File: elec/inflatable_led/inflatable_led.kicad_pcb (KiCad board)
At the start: 2 copper layers, 100.1 x 100 mm, 86 parts, among them J1 Header-Male-2.54_1x20, J2 Conn_01x02_Pin, J3 Conn_01x02_Pin, SW1 TS-1093C-A7B2-D1, U1 RP2040, U2 W25Q128JVSIQTR, U3 TPS61165DRVR, U4 BQ24040DSQR, U5 AMS1117-3.3, U6 F.0603.00026/P2-0603B1TS2-06T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, U7 SI2323DS, X1 X322512MSB4SI

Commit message: whole new circuit
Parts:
- removed BAT1, BAT2: BH-18650-A5BJ003, footprints:BAT-TH_BH-18650-A5BJ003
- removed C13: 10nF, Capacitor_SMD:C_0402_1005Metric
- removed D8, D9: MBR0540T1G, footprints:SOD-123_L2.8-W1.8-LS3.7-RD
- removed SW1: TS-1093C-A7B2-D1, footprints:SW-TH_TS-1093C-A7B3-D1
- removed TP_POWER_OR_1: TestPoint, TestPoint:TestPoint_Pad_D1.5mm
- added BT1: BH-18650-B1BA007, footprints:BAT-SMD_BH-18650-B1BA007, F.Cu at (101.4, 100.0)
- added BTBOOT1: TS-1187A-B-A-B, footprints:SW-SMD_4P-L5.1-W5.1-P3.70-LS6.5-TL-2, F.Cu at (123.8, 70.1)
- added BTUI1: TS-1187A-B-A-B, footprints:SW-SMD_4P-L5.1-W5.1-P3.70-LS6.5-TL-2, F.Cu at (101.4, 75.0)
- added C14: 47nF, Capacitor_SMD:C_0603_1608Metric, F.Cu at (114.4, 127.8)
- added C23: 10uF, Capacitor_SMD:C_0805_2012Metric, F.Cu at (110.4, 122.1)
- added C24: 10uF, Capacitor_SMD:C_0805_2012Metric, F.Cu at (117.1, 128.4)
- added C25: 1uF, Capacitor_SMD:C_0603_1608Metric, F.Cu at (125.0, 76.8)
- added C26: 1uF, Capacitor_SMD:C_0603_1608Metric, F.Cu at (125.0, 78.5)
- added CN1: S2B-PH-SM4-TB(LF)(SN), footprints:CONN-SMD_P2.00_S2B-PH-SM4-TB-LF-SN, F.Cu at (107.6, 140.0)
- added J4: USB4205-GF-A_REVA, footprints:GCT_USB4205-GF-A_REVA, F.Cu at (101.4, 57.8)
- added JP1: SolderJumper_3_Bridged12, Jumper:SolderJumper-3_P1.3mm_Bridged12_RoundedPad1.0x1.5mm, F.Cu at (93.2, 121.5)
- added JP2: SolderJumper_2_Open, Jumper:SolderJumper-2_P1.3mm_Open_TrianglePad1.0x1.5mm, F.Cu at (106.1, 74.9)
- added JP3: SolderJumper_3_Open, Jumper:SolderJumper-3_P2.0mm_Open_TrianglePad1.0x1.5mm, F.Cu at (123.6, 74.3)
- added L2: 1uH/3A, Inductor_SMD:L_1008_2520Metric, F.Cu at (110.8, 126.8)
- added Q1: 2N7002KW_R1_00001, footprints:SOT-323-3_L2.0-W1.3-P1.30-LS2.1-BR, F.Cu at (89.4, 128.2)
- added R17: 10K, Resistor_SMD:R_0402_1005Metric, F.Cu at (112.9, 129.5)
- added R18: 10K, Resistor_SMD:R_0402_1005Metric, F.Cu at (91.9, 124.1)
- added R19: 10k, Resistor_SMD:R_0603_1608Metric, F.Cu at (118.1, 71.7)
- added R20: 10K, Resistor_SMD:R_0402_1005Metric, F.Cu at (89.2, 130.1)
- added TP1: TestPoint, TestPoint:TestPoint_Pad_D1.0mm, F.Cu at (118.2, 74.5)
- added TP2: TestPoint, TestPoint:TestPoint_Pad_D1.0mm, F.Cu at (127.9, 77.6)
- added TP7: TestPoint, TestPoint:TestPoint_Pad_D1.0mm, F.Cu at (118.2, 76.6)
- added TP8: TestPoint, TestPoint:TestPoint_Pad_D1.0mm, F.Cu at (118.2, 78.7)
- added U8: TPS7A0233DQNR, footprints:X2SON-4_L1.0-W1.0-P0.65-TL-EP, F.Cu at (115.2, 132.4)
- C19: value 1uF -> 0.1uF; footprint Capacitor_SMD:C_0805_2012Metric -> Capacitor_SMD:C_0603_1608Metric
- C20, C21: value 100nF -> 1uF; footprint Capacitor_SMD:C_0402_1005Metric -> Capacitor_SMD:C_0805_2012Metric
- J1: value Header-Male-2.54_1x20 -> Conn_01x10; footprint footprints:HDR-TH_20P-P2.54-V-M-1 -> Connector_PinHeader_1.00mm:PinHeader_1x10_P1.00mm_Vertical
- R7: value 600R -> 10K
- U4: value BQ24040DSQR -> BQ25601DRTWR; footprint footprints:WSON-10_L2.0-W2.0-P0.40-BL-EP -> footprints:WQFN-24_L4.0-W4.0-P0.50-TL-EP2.7
- U5: value AMS1117-3.3 -> STM6601GU2BDM6F; footprint footprints:SOT-223-3_L6.5-W3.4-P2.30-LS7.0-BR -> Package_DFN_QFN:TDFN-12_2x3mm_P0.5mm
- moved H4 134.0 mm to (60.0, 22.0)
- moved H2 119.0 mm to (49.0, 23.1)
- moved H3 104.6 mm to (28.1, 21.5)
- moved D5 89.0 mm to (98.1, 141.5), turned to 90 degrees
- moved D6 88.7 mm to (95.3, 141.4), turned to -90 degrees
- moved TP6 75.2 mm to (57.3, 104.6)
- moved D7 67.0 mm to (92.6, 141.4)
- moved TPCC1 65.8 mm to (95.3, 62.2), turned to 180 degrees
- moved R10 64.2 mm to (97.1, 65.2), turned to 180 degrees
- moved D4 54.3 mm to (93.0, 134.7), turned to 90 degrees
- moved U5 52.6 mm to (121.4, 77.8), turned to 180 degrees
- moved H1 52.2 mm to (38.6, 23.4)
- moved USB2 49.7 mm to (114.1, 61.6), turned to 160 degrees
- moved R11 49.5 mm to (105.3, 62.3), turned to 0 degrees
- moved TPCC2 48.9 mm to (106.1, 59.6), turned to 180 degrees
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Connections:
- C19 pad 1: +BATT -> VCC
- C20 pad 1: /POWER_IN_OR -> VCC
- C22 pad 1: /ON_OFF_BT -> /PWR_ON
- J1 pad 1: Net-(U1-GPIO9) -> GND
- J1 pad 10: Net-(U1-GPIO18) -> /GPIO11
- J1 pad 2: Net-(U1-GPIO10) -> +3.3V
- J1 pad 3: Net-(U1-GPIO11) -> +BATT
- J1 pad 4: Net-(U1-GPIO12) -> VCC
- J1 pad 5: Net-(U1-GPIO13) -> VBUS
- J1 pad 6: Net-(U1-GPIO14) -> /PWR_EN
- J1 pad 7: Net-(U1-GPIO15) -> /GPIO8
- J1 pad 8: Net-(U1-GPIO16) -> /GPIO9
- J1 pad 9: Net-(U1-GPIO17) -> /GPIO10
- LED_CHG_2 pad 1: /CHG_CHG -> /CHG_STAT
- R15 pad 2: /ON_OFF_BT -> /PWR_ON
- R16 pad 1: Net-(U7-G) -> /LED_ON
- R16 pad 2: /LED_ON -> Net-(Q1-G)
- R7 pad 1: Net-(U4-ISET) -> /CHG_REGN
- R7 pad 2: GND -> Net-(U4-TS)
- R8 pad 1: +BATT -> VCC
- R9 pad 1: +BATT -> VCC
- TP_LED_ON1 pad 1: Net-(U7-G) -> /LED_ON
- U1 pad 11: unconnected-(U1-GPIO8-Pad11) -> /GPIO8
- U1 pad 12: Net-(U1-GPIO9) -> /GPIO9
- U1 pad 13: Net-(U1-GPIO10) -> /GPIO10
- U1 pad 14: Net-(U1-GPIO11) -> /GPIO11
- U1 pad 15: Net-(U1-GPIO12) -> /GPIO12
- U1 pad 16: Net-(U1-GPIO13) -> /GPIO13
- U1 pad 17: Net-(U1-GPIO14) -> /PWR_HOLD
- U1 pad 18: Net-(U1-GPIO15) -> /PWR_LOW
- U1 pad 2: unconnected-(U1-GPIO0-Pad2) -> /DIM_CTRL
- U1 pad 27: Net-(U1-GPIO16) -> /BTN1
- U1 pad 28: Net-(U1-GPIO17) -> /GPIO17
- U1 pad 29: Net-(U1-GPIO18) -> /GPIO18
- U1 pad 3: unconnected-(U1-GPIO1-Pad3) -> /LED_ON
- U1 pad 30: Net-(U1-GPIO19) -> unconnected-(U1-GPIO19-Pad30)
- U1 pad 31: Net-(U1-GPIO20) -> unconnected-(U1-GPIO20-Pad31)
- U1 pad 32: Net-(U1-GPIO21) -> unconnected-(U1-GPIO21-Pad32)
- U1 pad 34: Net-(U1-GPIO22) -> unconnected-(U1-GPIO22-Pad34)
- U1 pad 35: Net-(U1-GPIO23) -> unconnected-(U1-GPIO23-Pad35)
- U1 pad 36: Net-(U1-GPIO24) -> unconnected-(U1-GPIO24-Pad36)
- U1 pad 37: Net-(U1-GPIO25) -> unconnected-(U1-GPIO25-Pad37)
- U1 pad 38: Net-(U1-GPIO26_ADC0) -> unconnected-(U1-GPIO26_ADC0-Pad38)
- U1 pad 39: Net-(U1-GPIO27_ADC1) -> unconnected-(U1-GPIO27_ADC1-Pad39)
- U1 pad 4: unconnected-(U1-GPIO2-Pad4) -> /CHG_QON
- U1 pad 40: Net-(U1-GPIO28_ADC2) -> unconnected-(U1-GPIO28_ADC2-Pad40)
- U1 pad 5: /LED_ON -> /CHG_INT
- U1 pad 6: /DIM_CTRL -> /SDA
- U1 pad 7: /ON_OFF_BT -> /SCL
- U1 pad 8: unconnected-(U1-GPIO6-Pad8) -> /CHG_STAT
- U1 pad 9: unconnected-(U1-GPIO7-Pad9) -> /CHG_PG
- U4 pad 10: +BATT -> unconnected-(U4-NC-Pad10)
- U4 pad 11: GND -> Net-(U4-TS)
- U4 pad 2: Net-(U4-ISET) -> VBUS
- U4 pad 3: GND -> /CHG_PG
- U4 pad 4: unconnected-(U4-PRETERM-Pad4) -> /CHG_STAT
- U4 pad 5: /CHG_PG -> /SCL
- U4 pad 6: unconnected-(U4-NC-Pad6) -> /SDA
- U4 pad 7: VBUS -> /CHG_INT
- U4 pad 8: /CHG_CHG -> unconnected-(U4-NC-Pad8)
- U4 pad 9: unconnected-(U4-TS-Pad9) -> GND
- U5 pad 1: GND -> VCC
- U5 pad 2: +3.3V -> /PWR_SR
- U5 pad 3: /POWER_IN_OR -> Net-(U5-VREF)
- U5 pad 4: +3.3V -> /PWR_HOLD
- U7 pad 1: Net-(U7-G) -> Net-(Q1-D)
- U7 pad 2: +BATT -> Net-(JP1-C)
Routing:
- net +3.3V: track 222.6 -> 31.7 mm, vias 7 -> 15
- net VCC: track 0.00 -> 90.1 mm, vias 0 -> 9
- net /PWR_EN: track 0.00 -> 75.7 mm, vias 0 -> 2
- net /ON_OFF_BT: track 74.7 -> 0.00 mm, vias 1 -> 0
- net Net-(D4-K): track 82.1 -> 7.55 mm
- net /CHG_STAT: track 0.00 -> 61.3 mm
- net Net-(U1-GPIO9): track 60.3 -> 0.00 mm
- net /DIM_CTRL: track 112.7 -> 52.5 mm, vias 4 -> 2
- net /CHG_PG: track 4.18 -> 62.7 mm, vias 2 -> 0
- net /SCL: track 0.00 -> 58.5 mm
- net /LED_ON: track 113.8 -> 55.4 mm, vias 2 -> 0
- net Net-(U1-GPIO10): track 58.1 -> 0.00 mm
- net /SDA: track 0.00 -> 57.3 mm
- net /CHG_INT: track 0.00 -> 56.3 mm
- net /CHG_QON: track 0.00 -> 55.6 mm, vias 0 -> 2
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- added copper zone on F.Cu, net +3.3V
- added copper zone on In1.Cu, net +3.3V
- added copper zone on F.Cu, net +BATT
- added copper zone on In2.Cu, net +BATT
- added copper zone on In2.Cu, net VBUS
- added copper zone on In2.Cu, net VCC
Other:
- board size 100.1 x 100 mm -> 91.8 x 92 mm
- copper layers 2 -> 4
- board text added: "Boot"
- board text added: "Reset"

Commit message: update bom
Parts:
- C19: value 0.1uF -> 100nF; footprint Capacitor_SMD:C_0603_1608Metric -> Capacitor_SMD:C_0402_1005Metric
- C25, C26: footprint Capacitor_SMD:C_0603_1608Metric -> Capacitor_SMD:C_0805_2012Metric
- R19: footprint Resistor_SMD:R_0603_1608Metric -> Resistor_SMD:R_0402_1005Metric
- moved H3 149.8 mm to (131.4, 130.0)
- moved H4 108.6 mm to (71.4, 130.0)
- moved H1 103.8 mm to (131.4, 70.0)
- moved H2 52.0 mm to (71.4, 70.0)
- moved J3 0.60 mm to (130.6, 124.3)
- moved C1 0.57 mm to (94.6, 79.0)
- moved C25 0.55 mm to (124.9, 76.2)
- moved U5 0.51 mm to (121.3, 77.3)
- moved C5 0.50 mm to (80.3, 78.6)
- moved JP3 0.33 mm to (123.6, 74.0)
- moved C26 0.25 mm to (125.0, 78.2)
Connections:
- U1 pad 28: /GPIO17 -> unconnected-(U1-GPIO17-Pad28)
- U1 pad 29: /GPIO18 -> unconnected-(U1-GPIO18-Pad29)
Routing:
- net /PWR_ON: track 19.2 -> 38.3 mm, vias 0 -> 2
- net /QSPI_SS: track 58.8 -> 42.3 mm, vias 0 -> 2
- net +BATT: track 57.7 -> 50.3 mm, vias 31 -> 30
- net GND: track 44.0 -> 45.8 mm, vias 67 -> 68
- net /PWR_SR: track 9.45 -> 10.9 mm
- net /osc_in: track 10.5 -> 9.80 mm
- net /BTN1: track 39.0 -> 38.3 mm
- net /PWR_EN: track 75.7 -> 75.2 mm
- net VCC: track 90.1 -> 90.6 mm
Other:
- outline, holes or cut-outs redrawn

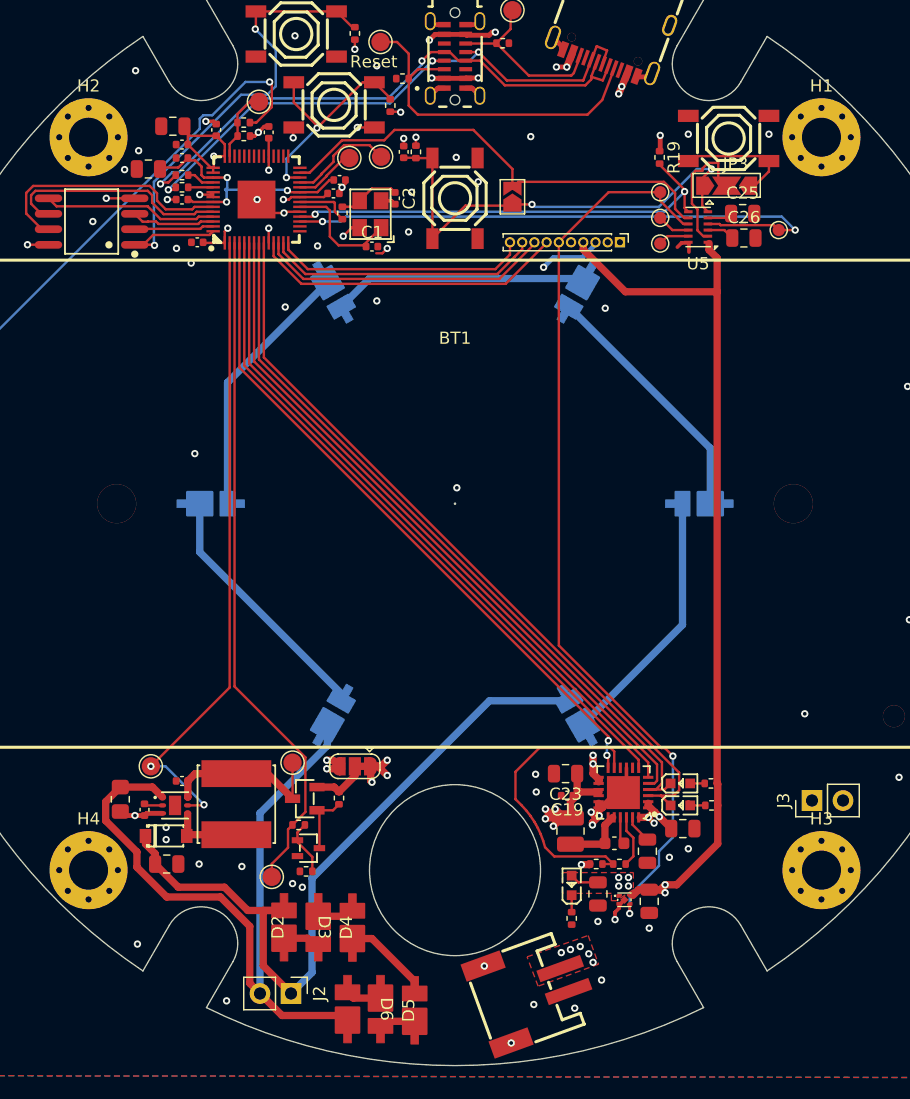
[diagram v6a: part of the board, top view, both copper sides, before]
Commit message: fix additional parts in BOM
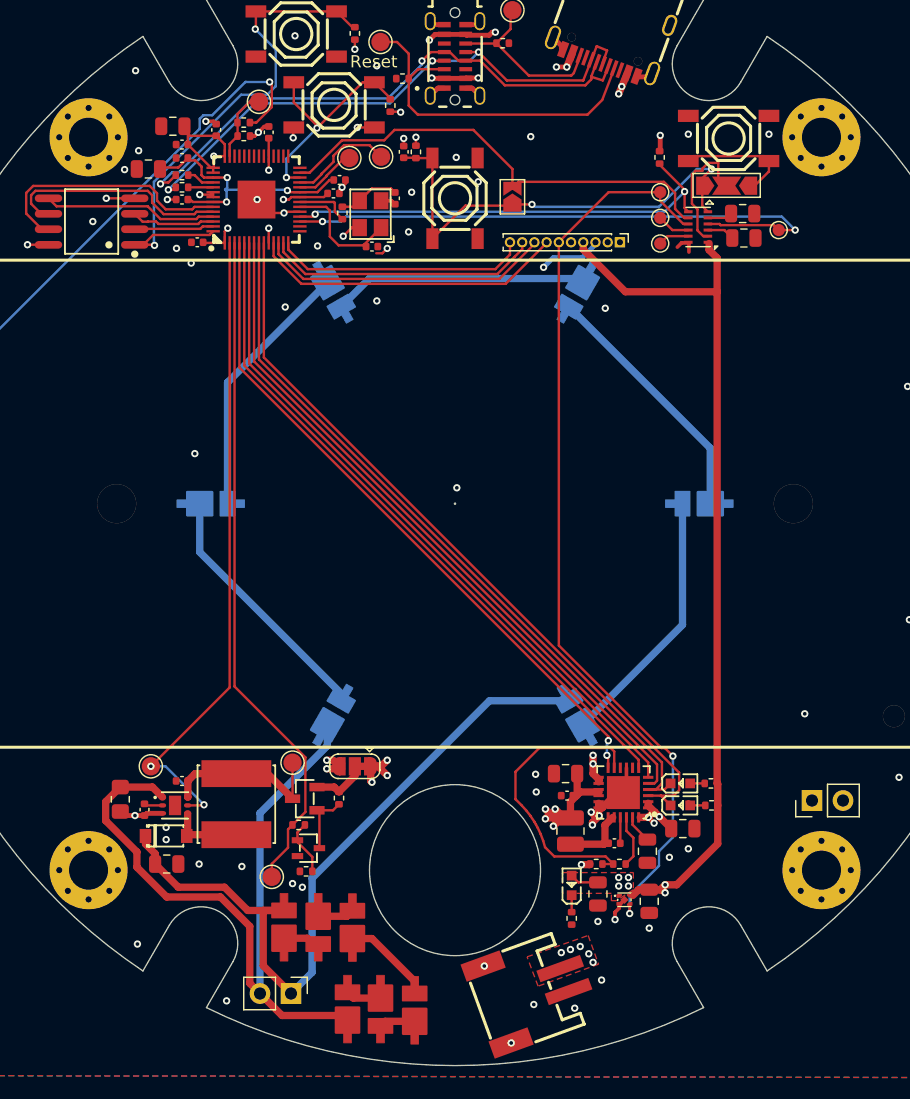
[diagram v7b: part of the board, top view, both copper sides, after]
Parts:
- C14: footprint Capacitor_SMD:C_0603_1608Metric -> Capacitor_SMD:C_0402_1005Metric
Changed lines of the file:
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@@
 			(at 0 -4.2 0)
 			(layer "F.SilkS")
+			(hide yes)
 			(effects
 				(font
@@
 			(at 0.725 -1.775 0)
 			(layer "F.SilkS")
+			(hide yes)
 			(effects
 				(font
@@
 			(at 0 -1.17 -90)
 			(layer "F.SilkS")
+			(hide yes)
 			(effects
 				(font
@@
 			(at 0 -1.68 0)
 			(layer "F.SilkS")
+			(hide yes)
 			(effects
 				(font
@@
 			(at 0 -1.16 180)
 			(layer "F.SilkS")
+			(hide yes)
 			(effects
 				(font
@@
 			(at 0 -3 180)
 			(layer "F.SilkS")
+			(hide yes)
 			(effects
 				(font
@@
 			(at 0 -13.55 0)
 			(layer "F.SilkS")
+			(hide yes)
 			(effects
 				(font
@@
 		)
 	)
-	(footprint "Capacitor_SMD:C_0603_1608Metric"
+	(footprint "Capacitor_SMD:C_0402_1005Metric"
 		(layer "F.Cu")
 		(at 114.42 127.8 180)
-		(descr "Capacitor SMD 0603 (1608 Metric), square (rectangular) end terminal, IPC_7351 nominal, (Body size source: IPC-SM-782 page 76, https://www.pcb-3d.com/wordpress/wp-content/uploads/ipc-sm-782a_amendment_1_and_2.pdf), generated with kicad-footprint-generator")
+		(descr "Capacitor SMD 0402 (1005 Metric), square (rectangular) end terminal, IPC_7351 nominal, (Body size source: IPC-SM-782 page 76, https://www.pcb-3d.com/wordpress/wp-content/uploads/ipc-sm-782a_amendment_1_and_2.pdf), generated with kicad-footprint-generator")
 		(tags "capacitor")
 		(property "Reference" "C14"
-			(at 0 -1.43 180)
+			(at 0 -1.16 180)
 			(layer "F.SilkS")
 			(hide yes)
@@
 		)
 		(property "Value" "47nF"
-			(at 0 1.43 180)
+			(at 0 1.16 180)
 			(layer "F.Fab")
 			(effects
@@
 			)
 		)
-		(property "Footprint" "Capacitor_SMD:C_0603_1608Metric"
+		(property "Footprint" "Capacitor_SMD:C_0402_1005Metric"
 			(at 0 0 180)
 			(unlocked yes)
@@
 			)
 		)
-		(property "LCSC Part" "C77012"
+		(property "LCSC Part" "C272875"
 			(at 0 0 180)
 			(unlocked yes)
@@
 		(attr smd)
 		(fp_line
-			(start -0.14058 0.51)
-			(end 0.14058 0.51)
+			(start -0.107836 0.36)
+			(end 0.107836 0.36)
 			(stroke
 				(width 0.12)
@@
 		)
 		(fp_line
-			(start -0.14058 -0.51)
-			(end 0.14058 -0.51)
+			(start -0.107836 -0.36)
+			(end 0.107836 -0.36)
 			(stroke
 				(width 0.12)
@@
 		)
 		(fp_line
-			(start 1.48 0.73)
-			(end -1.48 0.73)
+			(start 0.91 0.46)
+			(end -0.91 0.46)
 			(stroke
 				(width 0.05)
@@
 		)
 		(fp_line
-			(start 1.48 -0.73)
-			(end 1.48 0.73)
+			(start 0.91 -0.46)
+			(end 0.91 0.46)
 			(stroke
 				(width 0.05)
@@
 		)
 		(fp_line
-			(start -1.48 0.73)
-			(end -1.48 -0.73)
+			(start -0.91 0.46)
+			(end -0.91 -0.46)
 			(stroke
 				(width 0.05)
@@
 		)
 		(fp_line
-			(start -1.48 -0.73)
-			(end 1.48 -0.73)
+			(start -0.91 -0.46)
+			(end 0.91 -0.46)
 			(stroke
 				(width 0.05)
@@
 		)
 		(fp_line
-			(start 0.8 0.4)
-			(end -0.8 0.4)
+			(start 0.5 0.25)
+			(end -0.5 0.25)
 			(stroke
 				(width 0.1)
@@
 		)
 		(fp_line
-			(start 0.8 -0.4)
-			(end 0.8 0.4)
+			(start 0.5 -0.25)
+			(end 0.5 0.25)
 			(stroke
 				(width 0.1)
@@
 		)
 		(fp_line
-			(start -0.8 0.4)
-			(end -0.8 -0.4)
+			(start -0.5 0.25)
+			(end -0.5 -0.25)
 			(stroke
 				(width 0.1)
@@
 		)
 		(fp_line
-			(start -0.8 -0.4)
-			(end 0.8 -0.4)
+			(start -0.5 -0.25)
+			(end 0.5 -0.25)
 			(stroke
 				(width 0.1)
@@
 			(effects
 				(font
-					(size 0.4 0.4)
-					(thickness 0.06)
+					(size 0.25 0.25)
+					(thickness 0.04)
 				)
 			)
 		)
 		(pad "1" smd roundrect
-			(at -0.775 0 180)
-			(size 0.9 0.95)
+			(at -0.48 0 180)
+			(size 0.56 0.62)
 			(layers "F.Cu" "F.Paste" "F.Mask")
 			(roundrect_rratio 0.25)
@@
 		)
 		(pad "2" smd roundrect
-			(at 0.775 0 180)
-			(size 0.9 0.95)
+			(at 0.48 0 180)
+			(size 0.56 0.62)
 			(layers "F.Cu" "F.Paste" "F.Mask")
 			(roundrect_rratio 0.25)
@@
 			(pintype "passive")
 		)
-		(model "${KICAD8_3DMODEL_DIR}/Capacitor_SMD.3dshapes/C_0603_1608Metric.wrl"
+		(model "${KICAD8_3DMODEL_DIR}/Capacitor_SMD.3dshapes/C_0402_1005Metric.wrl"
 			(offset
 				(xyz 0 0 0)
@@
 		(sheetname "Root")
 		(sheetfile "inflatable_led.kicad_sch")
-		(attr smd dnp)
+		(attr smd)
 		(fp_line
 			(start -0.153641 0.38)
@@
 			(at 0 -4.2 0)
 			(layer "F.SilkS")
+			(hide yes)
 			(effects
 				(font
@@
 			(at 0 -1.68 180)
 			(layer "F.SilkS")
+			(hide yes)
 			(effects
 				(font
@@
 			(at 0 -4.2 0)
 			(layer "F.SilkS")
+			(hide yes)
 			(effects
 				(font
@@
 			(at 0 -2.33 -90)
 			(layer "F.SilkS")
+			(hide yes)
 			(effects
 				(font
@@
 			(unlocked yes)
 			(layer "F.SilkS")
+			(hide yes)
 			(effects
 				(font
@@
 			(at 0 -4.2 0)
 			(layer "F.SilkS")
+			(hide yes)
 			(effects
 				(font
@@
 			)
 		)
-		(property "LCSC Part" "C21353"
+		(property "LCSC Part" "C109213"
 			(at 0 0 0)
 			(unlocked yes)
@@
 			(unlocked yes)
 			(layer "F.SilkS")
+			(hide yes)
 			(effects
 				(font
@@
 			(at 0 -1.68 0)
 			(layer "F.SilkS")
+			(hide yes)
 			(effects
 				(font
@@
 			(at 0 -1.16 0)
 			(layer "F.SilkS")
+			(hide yes)
 			(effects
 				(font
@@
 			(at 0 -2.33 90)
 			(layer "F.SilkS")
+			(hide yes)
 			(effects
 				(font
@@
 			(unlocked yes)
 			(layer "F.SilkS")
+			(hide yes)
 			(effects
 				(font
@@
 			(at 0 -1.16 90)
 			(layer "F.SilkS")
+			(hide yes)
 			(effects
 				(font
@@
 			(unlocked yes)
 			(layer "F.SilkS")
+			(hide yes)
 			(effects
 				(font
@@
 			(unlocked yes)
 			(layer "F.SilkS")
+			(hide yes)
 			(effects
 				(font
@@
 	)
 	(segment
-		(start 114.905 127.51)
-		(end 115.195 127.8)
-		(width 0.2)
-		(layer "F.Cu")
-		(net 11)
-	)
-	(segment

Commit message: final tweaks
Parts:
- moved U2 0.20 mm to (71.6, 76.7)
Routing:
- net /QSPI_SCLK: track 18.8 -> 19.4 mm
- net /QSPI_SD3: track 20.8 -> 21.4 mm
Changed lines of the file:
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@@
 	(footprint "footprints:SOIC-8_L5.3-W5.3-P1.27-LS8.0-BL"
 		(layer "F.Cu")
-		(at 71.62 76.9 90)
+		(at 71.62 76.7 90)
 		(property "Reference" "U2"
 			(at 0 -7.53 -90)
@@
 	)
 	(segment
+		(start 75.15 75)
+		(end 73.47 75)
+		(width 0.2)
+		(layer "F.Cu")
+		(net 1)
+	)
+	(segment
 		(start 87.37 76.2)
 		(end 86.22 76.2)
@@
 	)
 	(segment
+		(start 73.47 75)
+		(end 73.22 74.75)
+		(width 0.2)
+		(layer "F.Cu")
+		(net 1)
+	)
+	(segment
 		(start 112.82 125.55)
 		(end 112.52 125.25)
@@
 	)
 	(segment
-		(start 75.15 75)
-		(end 72.82 75)
-		(width 0.2)
-		(layer "F.Cu")
-		(net 1)
-	)
-	(segment
 		(start 144.2 108.28)
 		(end 144.7 107.78)
@@
 	)
 	(via
-		(at 72.82 75)
+		(at 73.22 74.75)
 		(size 0.6)
 		(drill 0.3)
@@
 	)
 	(segment
-		(start 68.745 75.655)
+		(start 68.59 75.5)
 		(end 68.09 75)
 		(width 0.2)
@@
 	)
 	(segment
-		(start 80.388628 76.5)
-		(end 80.188628 76.7)
+		(start 80.188628 76.7)
+		(end 77.42 76.7)
 		(width 0.2)
 		(layer "F.Cu")
@@
 	)
 	(segment
-		(start 80.188628 76.7)
-		(end 77.259741 76.7)
+		(start 80.388628 76.5)
+		(end 80.188628 76.7)
 		(width 0.2)
 		(layer "F.Cu")
@@
 	)
 	(segment
-		(start 77.259741 76.7)
-		(end 76.214741 75.655)
+		(start 77.42 76.7)
+		(end 76.22 75.5)
 		(width 0.2)
 		(layer "F.Cu")
@@
 	)
 	(segment
-		(start 76.214741 75.655)
-		(end 68.745 75.655)
+		(start 76.22 75.5)
+		(end 68.59 75.5)
 		(width 0.2)
 		(layer "F.Cu")
@@
 	)
 	(segment
-		(start 66.265 76.245)
-		(end 67.55 77.53)
+		(start 76.975 75.189314)
+		(end 76.975 74.355)
 		(width 0.2)
 		(layer "F.Cu")
@@
 	)
 	(segment
-		(start 76.975 75.189314)
-		(end 76.975 74.579573)
+		(start 79.857256 75.9)
+		(end 77.685686 75.9)
 		(width 0.2)
 		(layer "F.Cu")
@@
 	)
 	(segment
-		(start 66.835 73.985)
-		(end 66.265 74.555)
+		(start 80.057256 75.7)
+		(end 79.857256 75.9)
 		(width 0.2)
 		(layer "F.Cu")
@@
 	)
 	(segment
-		(start 66.265 74.555)
-		(end 66.265 76.245)
+		(start 76.975 74.355)
+		(end 76.22 73.6)
 		(width 0.2)
 		(layer "F.Cu")
@@
 	)
 	(segment
-		(start 67.55 77.53)
-		(end 68.09 77.53)
+		(start 66.265 74.355)
+		(end 66.265 76.245)
 		(width 0.2)
 		(layer "F.Cu")
@@
 	)
 	(segment
-		(start 79.857256 75.9)
-		(end 77.685686 75.9)
+		(start 81.57 75.7)
+		(end 80.057256 75.7)
 		(width 0.2)
 		(layer "F.Cu")
@@
 	)
 	(segment
-		(start 77.685686 75.9)
-		(end 76.975 75.189314)
+		(start 67.55 77.53)
+		(end 68.09 77.53)
 		(width 0.2)
 		(layer "F.Cu")
@@
 	)
 	(segment
-		(start 76.975 74.579573)
-		(end 76.380426 73.985)
+		(start 77.685686 75.9)
+		(end 76.975 75.189314)
 		(width 0.2)
 		(layer "F.Cu")
@@
 	)
 	(segment
-		(start 76.380426 73.985)
-		(end 66.835 73.985)
+		(start 76.22 73.6)
+		(end 67.02 73.6)
 		(width 0.2)
 		(layer "F.Cu")
@@
 	)
 	(segment
-		(start 80.057256 75.7)
-		(end 79.857256 75.9)
+		(start 66.265 76.245)
+		(end 67.55 77.53)
 		(width 0.2)
 		(layer "F.Cu")
@@
 	)
 	(segment
-		(start 81.57 75.7)
-		(end 80.057256 75.7)
+		(start 67.02 73.6)
+		(end 66.265 74.355)
 		(width 0.2)
 		(layer "F.Cu")
@@
 	)
 	(segment
-		(start 67.025259 74.385)
-		(end 66.665 74.745259)
+		(start 76.575 74.429738)
+		(end 76.145262 74)
 		(width 0.2)
 		(layer "F.Cu")
@@
 	)
 	(segment
-		(start 81.57 76.1)
-		(end 80.222942 76.1)
+		(start 76.575 75.355)
+		(end 76.575 74.429738)
 		(width 0.2)
 		(layer "F.Cu")
@@
 	)
 	(segment
-		(start 66.665 74.745259)
-		(end 66.665 75.445)
+		(start 80.022942 76.3)
+		(end 77.52 76.3)
 		(width 0.2)
 		(layer "F.Cu")
@@
 	)
 	(segment
-		(start 66.665 75.445)
-		(end 67.49 76.27)
+		(start 77.52 76.3)
+		(end 76.575 75.355)
 		(width 0.2)
 		(layer "F.Cu")
@@
 	)
 	(segment
-		(start 76.575 75.355)
-		(end 76.575 74.745259)
+		(start 66.665 74.455)
+		(end 66.665 75.445)
 		(width 0.2)
 		(layer "F.Cu")
@@
 	)
 	(segment
-		(start 76.214741 74.385)
-		(end 67.025259 74.385)
+		(start 66.665 75.445)
+		(end 67.49 76.27)
 		(width 0.2)
 		(layer "F.Cu")
@@
 	)
 	(segment
-		(start 76.575 74.745259)
-		(end 76.214741 74.385)
+		(start 76.145262 74)
+		(end 67.12 74)
 		(width 0.2)
 		(layer "F.Cu")
@@
 	)
 	(segment
-		(start 77.52 76.3)
-		(end 76.575 75.355)
+		(start 67.12 74)
+		(end 66.665 74.455)
 		(width 0.2)
 		(layer "F.Cu")
@@
 	)
 	(segment
-		(start 80.022942 76.3)
-		(end 77.52 76.3)
+		(start 81.57 76.1)
+		(end 80.222942 76.1)
 		(width 0.2)
 		(layer "F.Cu")
@@
 	)
 	(segment
-		(start 81.57 76.9)
-		(end 80.554314 76.9)
-		(width 0.2)
-		(layer "F.Cu")
-		(net 35)
-	)
-	(segment
-		(start 80.354313 77.1)
-		(end 77.094056 77.1)
-		(width 0.2)
-		(layer "F.Cu")
-		(net 35)
-	)
-	(segment
-		(start 76.214741 76.915)
-		(end 75.795 76.915)
+		(start 80.554314 76.9)
+		(end 80.354313 77.1)
 		(width 0.2)
 		(layer "F.Cu")
@@
 	)
 	(segment
-		(start 76.229741 76.9)
-		(end 76.214741 76.915)
+		(start 77.094056 77.1)
+		(end 76.644056 76.65)
 		(width 0.2)
 		(layer "F.Cu")
@@
 	)
 	(segment
-		(start 77.094056 77.1)
-		(end 76.894056 76.9)
+		(start 75.53 76.65)
+		(end 75.15 76.27)
 		(width 0.2)
 		(layer "F.Cu")
@@
 	)
 	(segment
-		(start 76.894056 76.9)
-		(end 76.229741 76.9)
+		(start 80.354313 77.1)
+		(end 77.094056 77.1)
 		(width 0.2)
 		(layer "F.Cu")
@@
 	)
 	(segment
-		(start 75.795 76.915)
-		(end 75.15 76.27)
+		(start 76.644056 76.65)
+		(end 75.53 76.65)
 		(width 0.2)
 		(layer "F.Cu")
@@
 	)
 	(segment
-		(start 80.554314 76.9)
-		(end 80.354313 77.1)
+		(start 81.57 76.9)
+		(end 80.554314 76.9)
 		(width 0.2)
 		(layer "F.Cu")
